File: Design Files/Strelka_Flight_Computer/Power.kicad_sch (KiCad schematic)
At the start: 28 parts, among them J1 2-3S_LiPo_LARGE_HOLE_XT-30, Q1 ??, Q2 ??, U1 FP6276BXR-G1, U2 AP9101CK6, U3 AMS1117-3.3

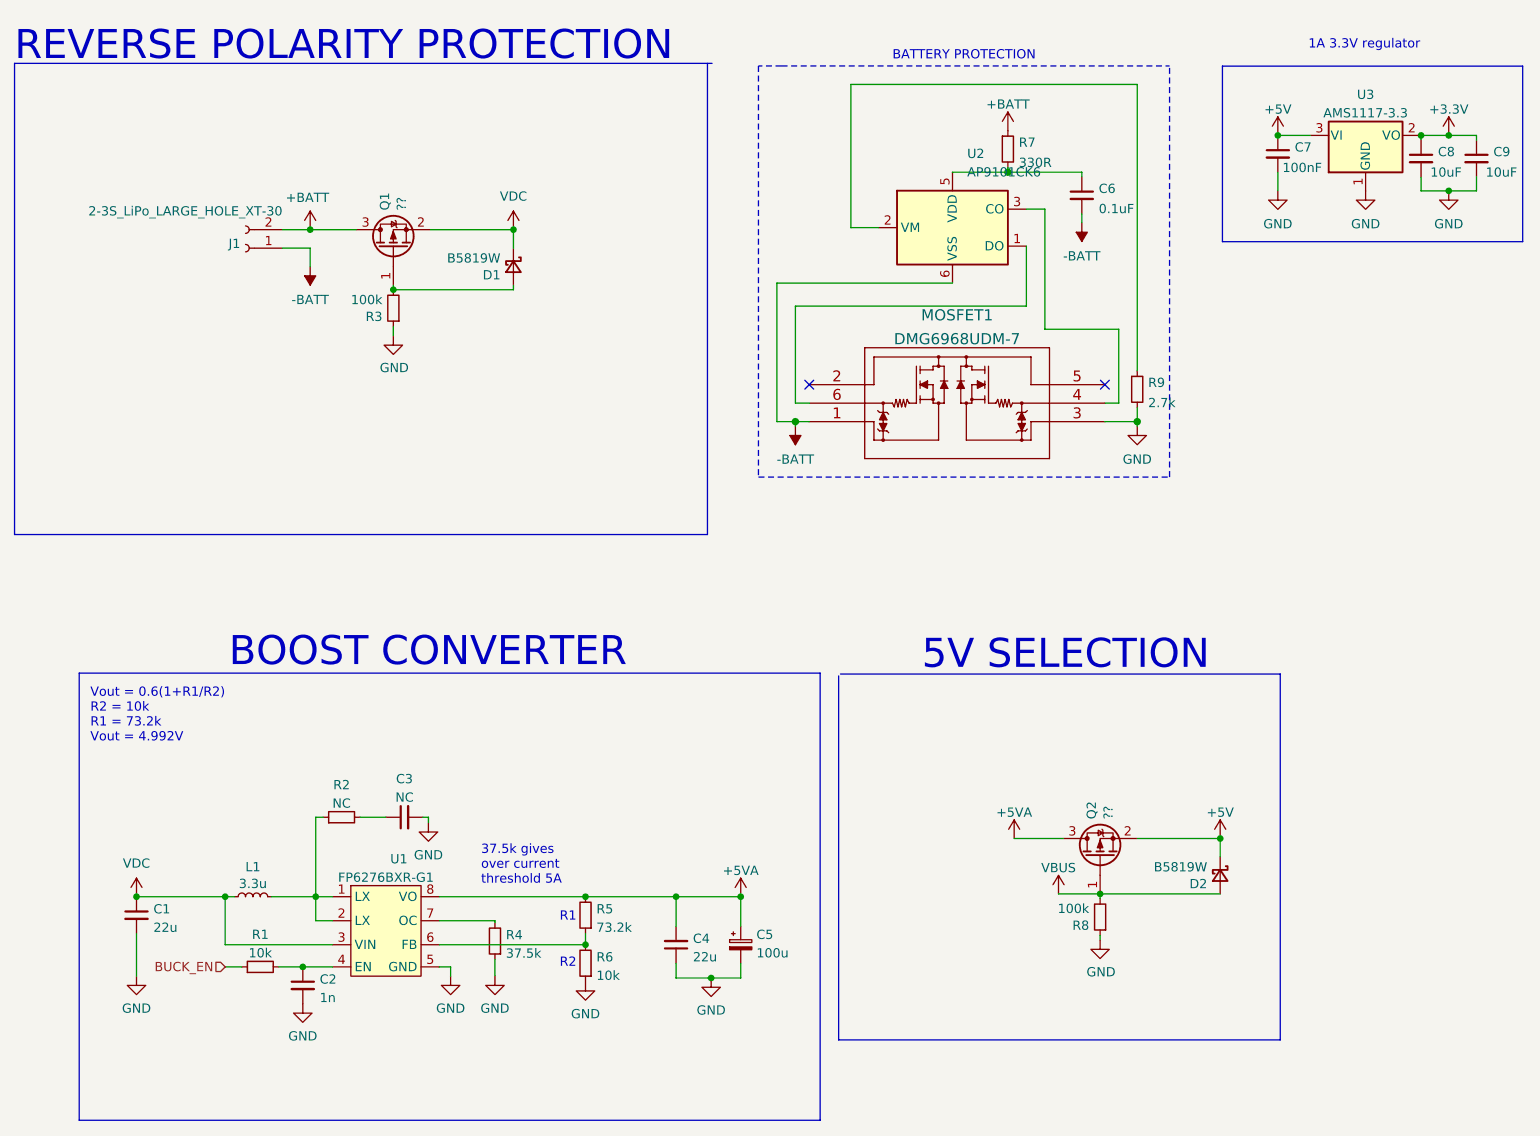
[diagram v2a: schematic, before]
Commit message: Added power board, almost finished Strelka schematic
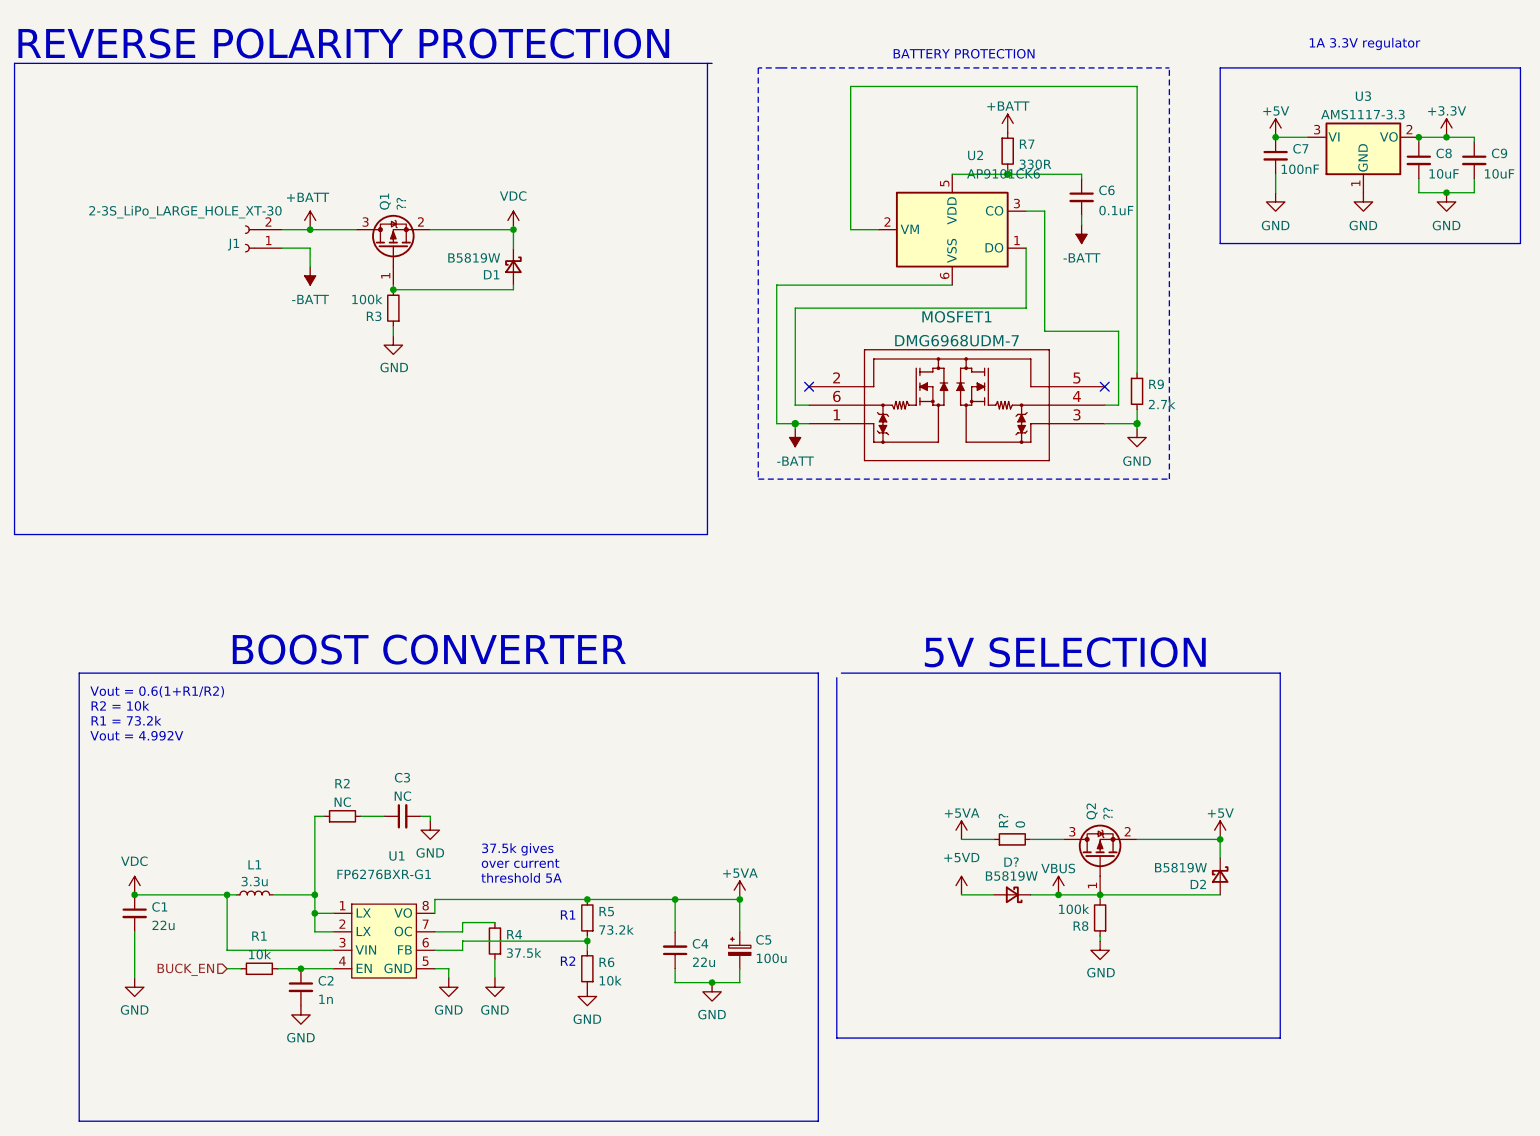
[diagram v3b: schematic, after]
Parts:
- added D?: B5819W, Diode_SMD:D_SOD-123, symbol Device:D_Schottky_Small
- added R?: 0, Resistor_SMD:R_0603_1608Metric, symbol Device:R_Small
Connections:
- net +5VA: now also R?.1; no longer Q2.3 (D)
- net VBUS: now also D?.1 (K)
- new net: Q2.3 (D), R?.2
- new net +5VD: D?.2 (A)
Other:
- moved on the sheet: C4, C5, R6, U1

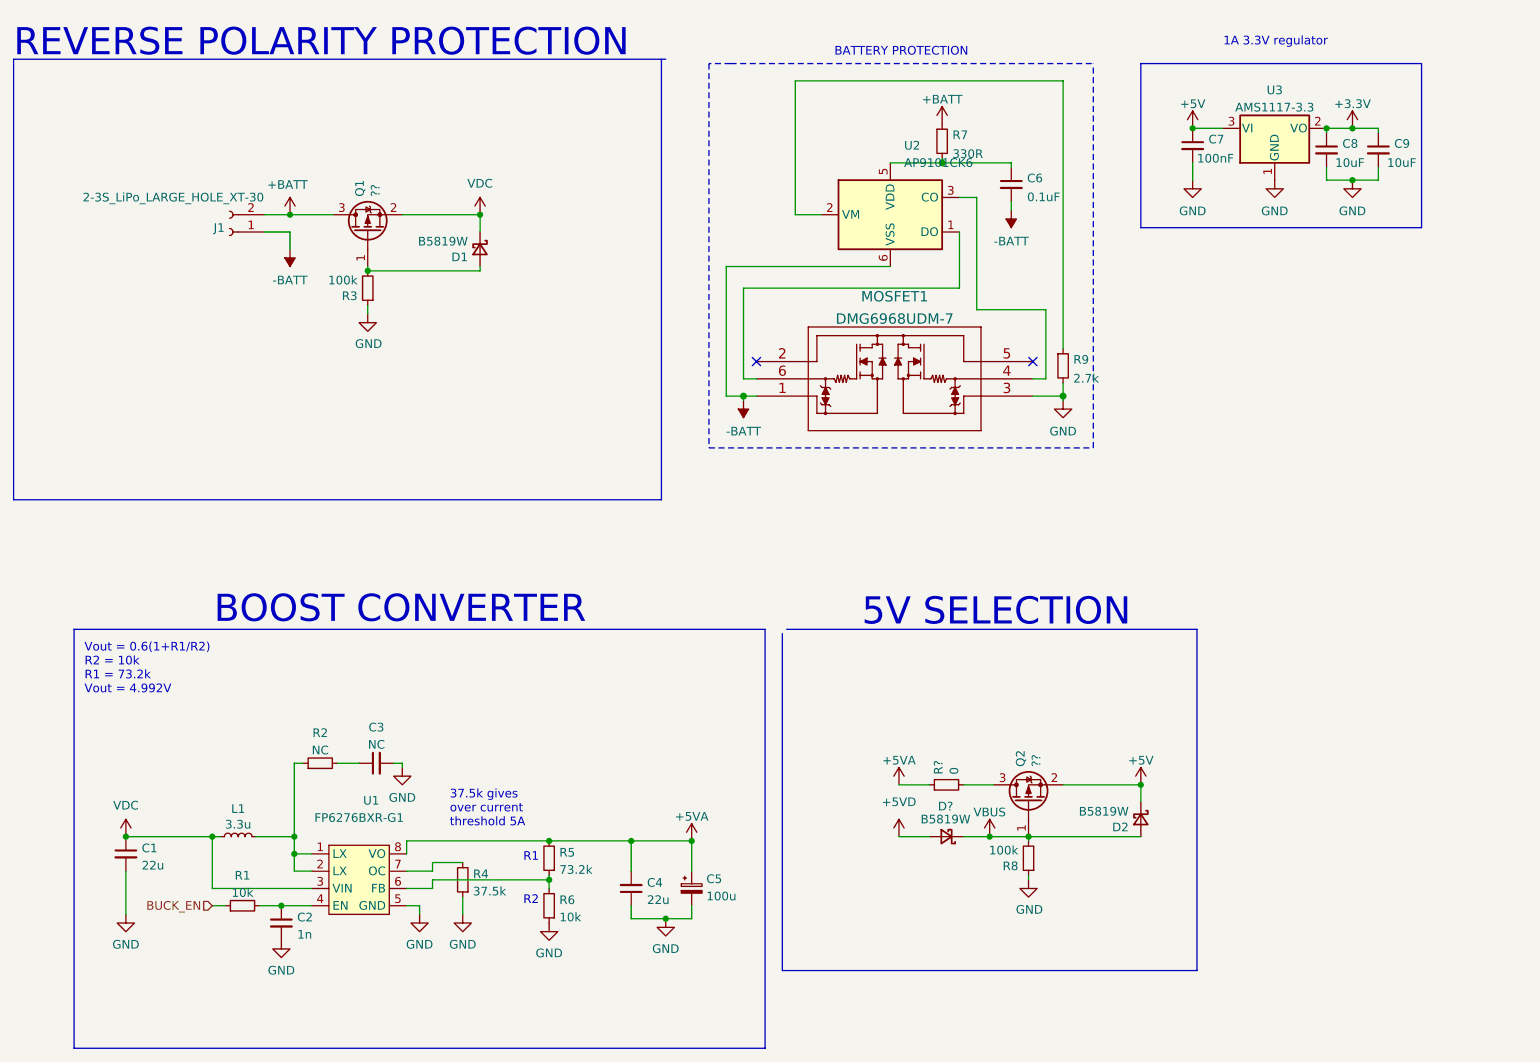
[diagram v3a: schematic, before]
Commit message: Added motor driver to power board
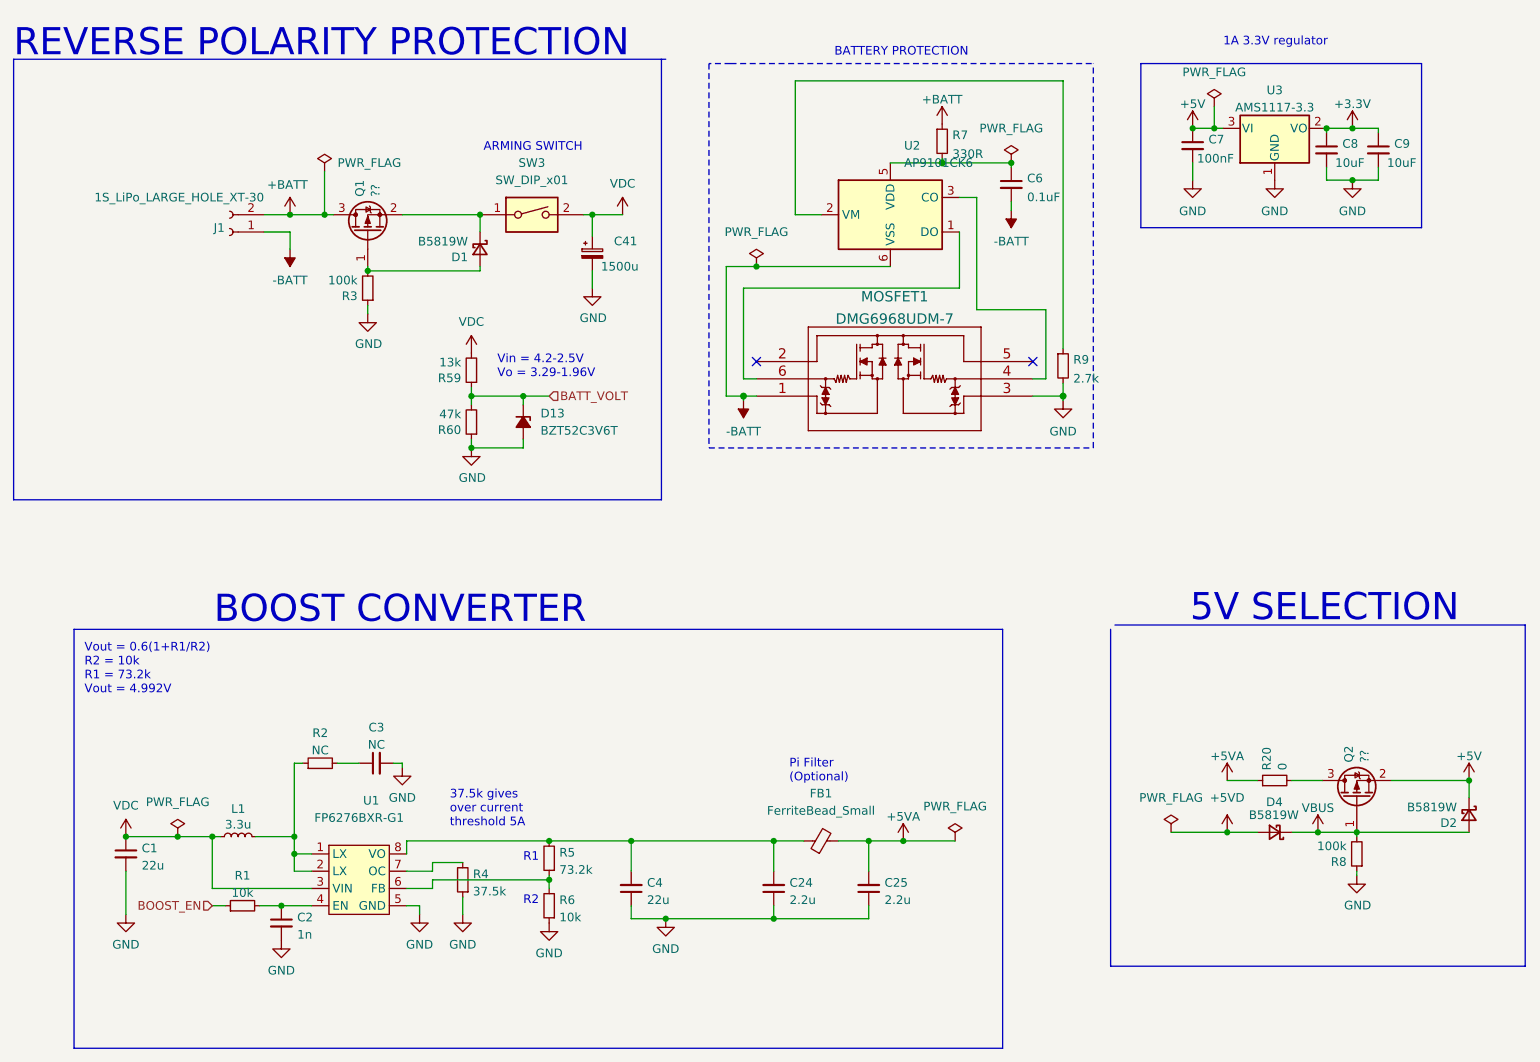
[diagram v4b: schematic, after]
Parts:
- removed C5: 100u, symbol Device:C_Polarized_Small
- added C24, C25: 2.2u, Capacitor_SMD:C_0603_1608Metric, symbol Device:C_Small
- added C41: 1500u, Capacitor_THT:C_Radial_D8.0mm_H11.5mm_P3.50mm, symbol Device:C_Polarized_Small
- added D13: BZT52C3V6T, Diode_SMD:D_SOD-523, symbol Device:D_Zener_Small_Filled
- added FB1: FerriteBead_Small, Inductor_SMD:L_0603_1608Metric, symbol Device:FerriteBead_Small
- added R59: 13k, Resistor_SMD:R_0603_1608Metric, symbol Device:R_Small
- added R60: 47k, Resistor_SMD:R_0603_1608Metric, symbol Device:R_Small
- added SW3: SW_DIP_x01, symbol Switch:SW_DIP_x01
- J1: value 2-3S_LiPo_LARGE_HOLE_XT-30 -> 1S_LiPo_LARGE_HOLE_XT-30
- gave numbers to parts that had none: 2
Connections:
- net +5VA: now also C25.2, FB1.2; no longer C4.2, R5.2, U1.8 (VO)
- net GND: now also C24.1, C25.1, C41.2, D13.2 (A), R60.1
- net VDC: now also C41.1, R59.2, SW3.2; no longer D1.1 (K), Q1.2 (S)
- net BUCK_EN renamed BOOST_EN
- new net: C24.2, C4.2, FB1.1, R5.2, U1.8 (VO)
- new net: D1.1 (K), Q1.2 (S), SW3.1
- new net BATT_VOLT: D13.1 (K), R59.1, R60.2
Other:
- note added: "ARMING SWITCH"
- note added: "Pi Filter (Optional)"
- note added: "Vin = 4.2-2.5V Vo = 3.29-1.96V"
- moved on the sheet: D2, D4, Q2, R20, R8

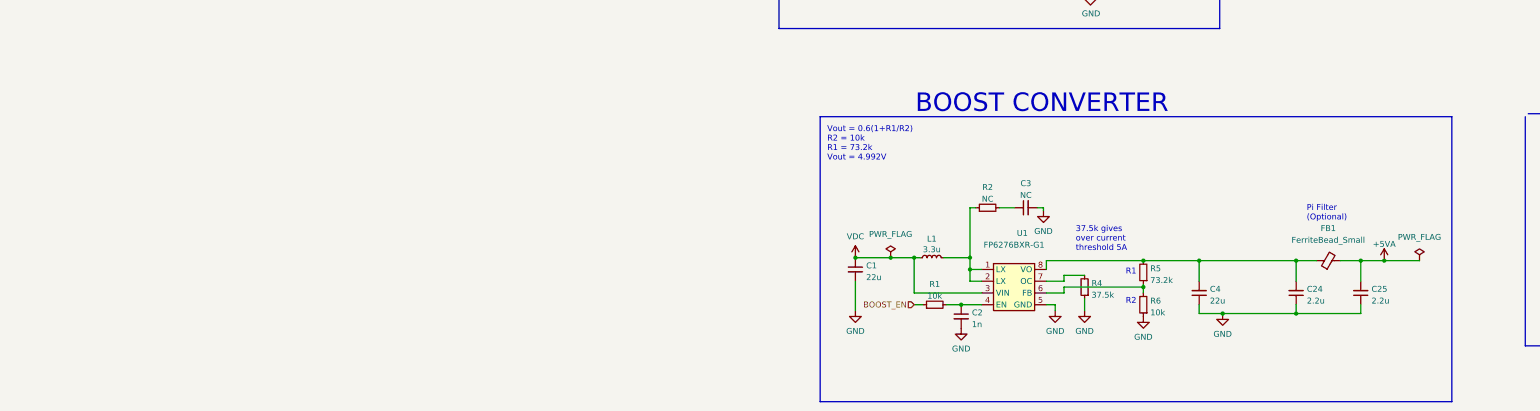
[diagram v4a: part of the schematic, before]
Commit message: Changed boost converter
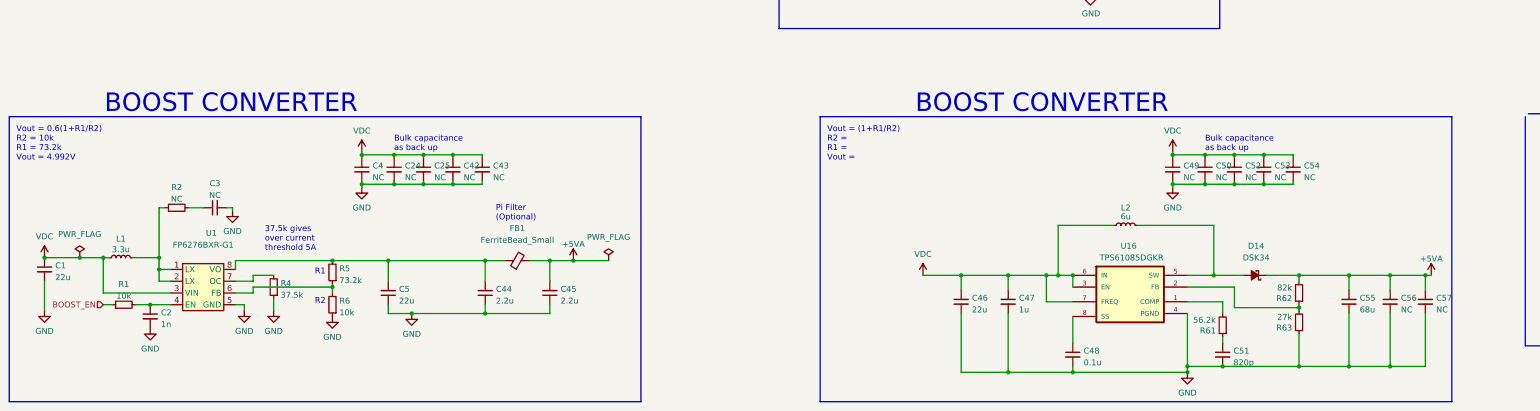
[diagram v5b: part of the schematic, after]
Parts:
- added C42, C43, C49, C50, C52, C53, C54, C56, C57: NC, Capacitor_SMD:C_0603_1608Metric, symbol Device:C_Small
- added C44, C45: 2.2u, Capacitor_SMD:C_0603_1608Metric, symbol Device:C_Small
- added C46, C5: 22u, Capacitor_SMD:C_0603_1608Metric, symbol Device:C_Small
- added C47: 1u, Capacitor_SMD:C_0603_1608Metric, symbol Device:C_Small
- added C48: 0.1u, Capacitor_SMD:C_0603_1608Metric, symbol Device:C_Small
- added C51: 820p, Capacitor_SMD:C_0603_1608Metric, symbol Device:C_Small
- added C55: 68u, Capacitor_SMD:C_0603_1608Metric, symbol Device:C_Small
- added D14: DSK34, Diode_SMD:D_SOD-123, symbol Device:D_Schottky_Small_Filled
- added L2: 6u, https:__datasheet.lcsc.com_lcsc_2105092345_BOURNS-SRP5030T-6R8M_C1329837.pdf, symbol Device:L_Small
- added R61: 56.2k, Resistor_SMD:R_0603_1608Metric, symbol Device:R_Small
- added R62: 82k, Resistor_SMD:R_0603_1608Metric, symbol Device:R_Small
- added R63: 27k, Resistor_SMD:R_0603_1608Metric, symbol Device:R_Small
- added U16: TPS61085DGKR, Footprints:SOP65P490X110-8N, symbol TPS61085DGKR:TPS61085DGKR
- C24, C25: value 2.2u -> NC
- C4: value 22u -> NC
- SW3: footprint (none) -> Footprints:SM02BGHSTBLFSN
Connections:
- net +5VA: now also C45.2, C55.1, C56.1, C57.1, D14.1 (K), R62.2; no longer C25.2
- net GND: now also C24.2, C25.2, C4.2, C42.2, C43.2, C44.1, C45.1, C46.2, C47.2, C48.2, C49.2, C5.1, C50.2, C51.2, C52.2, C53.2, C54.2, C55.2, C56.2, C57.2, R63.1, U16.4 (PGND); no longer C24.1, C25.1, C4.1
- net VDC: now also C24.1, C25.1, C4.1, C42.1, C43.1, C46.1, C47.1, C49.1, C50.1, C52.1, C53.1, C54.1, L2.1, U16.3 (EN), U16.6 (IN), U16.7 (FREQ)
- net at FB1.1, R5.2, U1.8 (VO): now also C44.2, C5.2; no longer C24.2, C4.2
- new net: C48.1, U16.8 (SS)
- new net: R62.1, R63.2, U16.2 (FB)
- new net: C51.1, R61.1
- new net: R61.2, U16.1 (COMP)
- new net: D14.2 (A), L2.2, U16.5 (SW)
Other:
- note added: "Bulk capacitance as back up"
- note added: "Vout = (1+R1/R2) R2 = R1 = Vout ="
